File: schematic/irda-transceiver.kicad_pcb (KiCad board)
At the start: 2 copper layers, 60 x 40 mm, 31 parts, among them J1 Conn_01x03_Pin, J2 Conn_01x03_Pin, J3 Conn_01x03_Pin, J4 Conn_01x03_Pin, J5 Conn_01x03_Pin, J6 Conn_01x03_Pin, J7 Conn_01x06_Pin, U1 MCP2120-I/P, U2 TFDU4101-TT3, Y1 7.3728 MHz

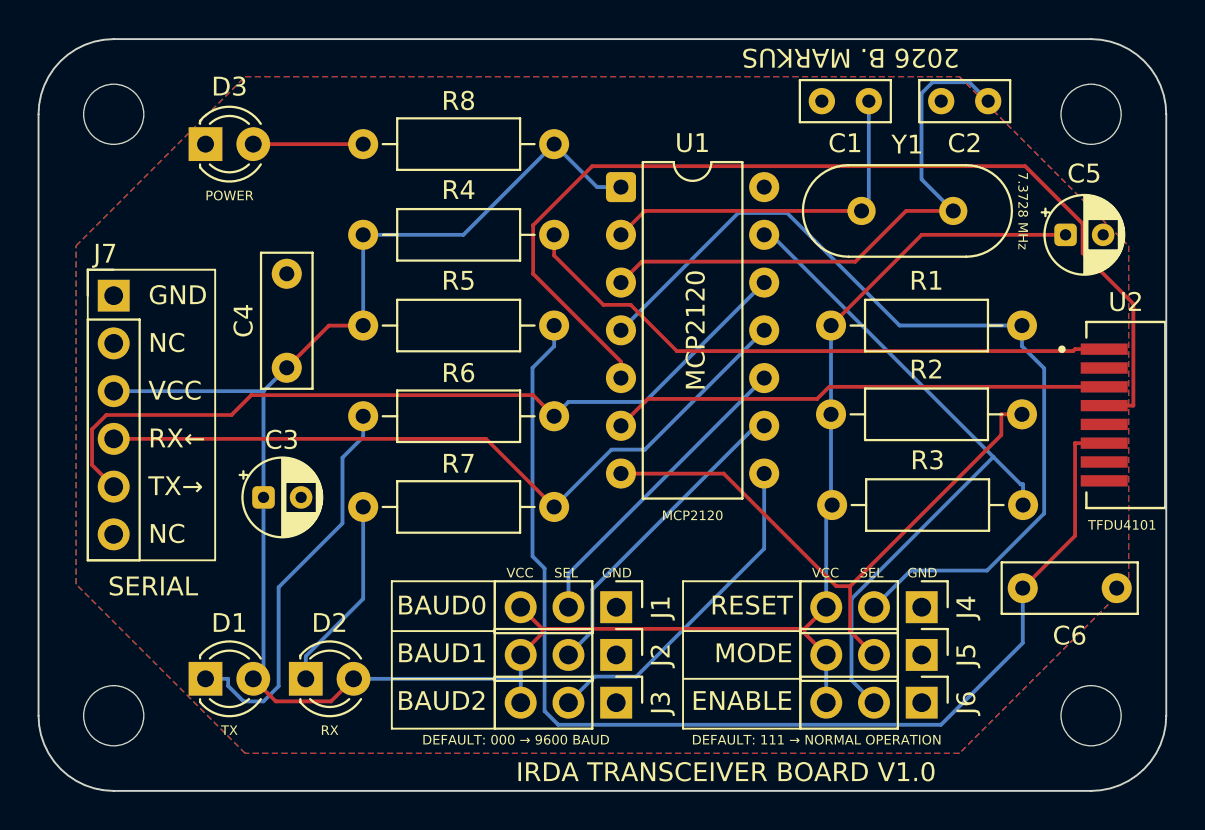
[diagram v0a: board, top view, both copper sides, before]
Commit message: PCB traces and silkscreen refined
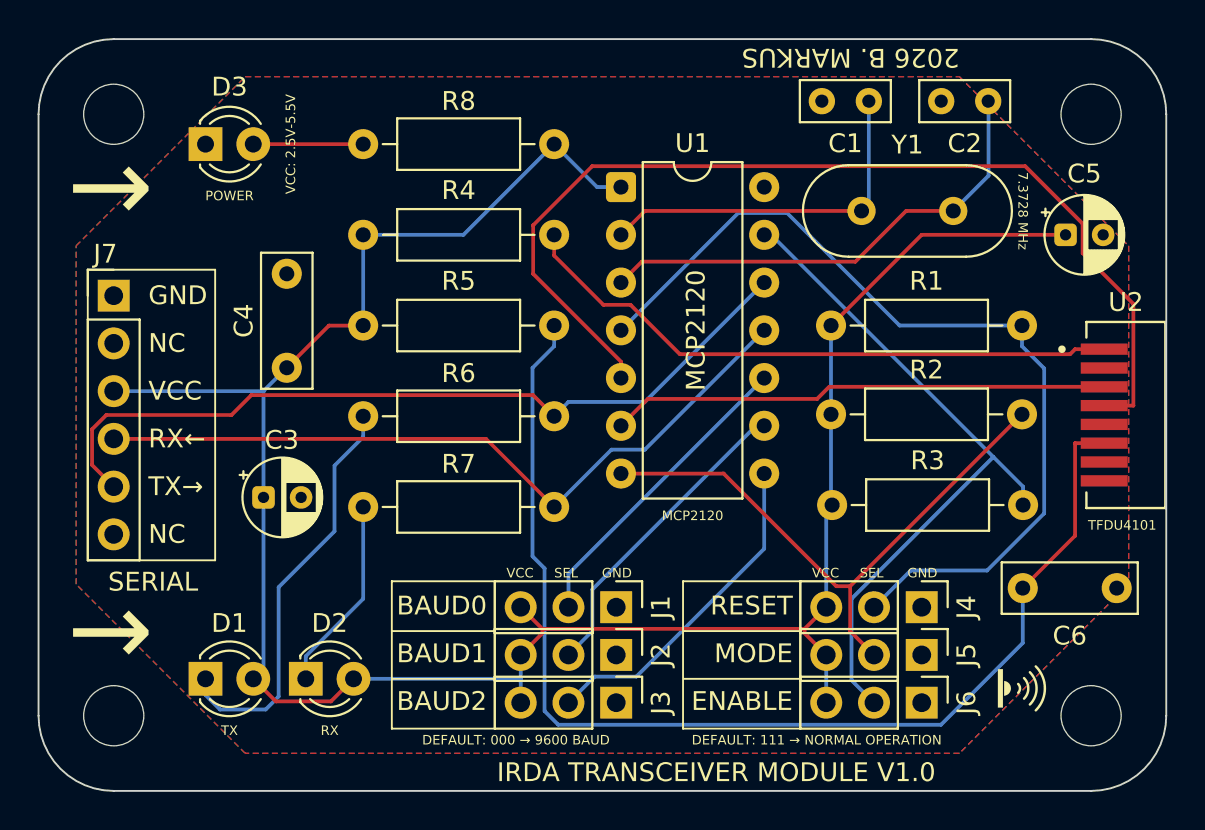
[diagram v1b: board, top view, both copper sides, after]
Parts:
- added G1: LOGO, LOGO, F.Cu at (52.3, 34.5)
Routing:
- net Net-(U1-OSC2): track 30.4 -> 25.9 mm
- net Net-(D1-K): track 21.2 -> 22.1 mm
- net Net-(J5-Pin_2): track 32.4 -> 31.8 mm
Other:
- board text added: "IRDA TRANSCEIVER MODULE V1.0"
- board text added: "VCC: 2.5V-5.5V"
- board text added: "→"
- board text removed: "IRDA TRANSCEIVER BOARD V1.0"
